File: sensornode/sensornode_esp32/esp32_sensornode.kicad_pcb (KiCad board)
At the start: 2 copper layers, 70 x 33 mm, 38 parts, among them J1 Conn_01x06_Female, J2 Conn_01x07_Male, J3 Micro_SD_Card, J4 USB_B_Mini, J5 Conn_01x02_Male, J6 Conn_02x03_Odd_Even, J7 Conn_02x03_Odd_Even, Q1 NDS3332P, Q2 NDS3332P, Q3 NDS3332P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

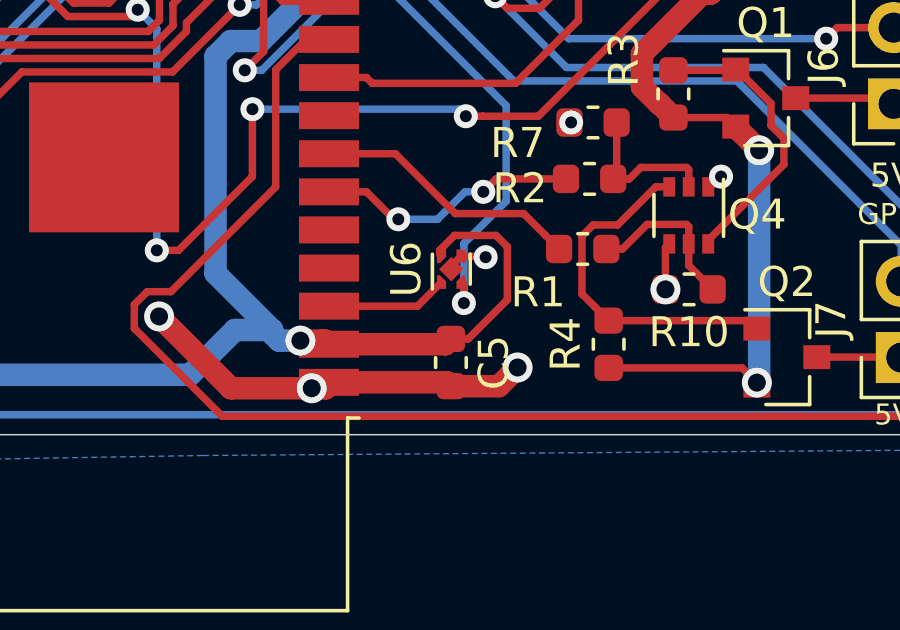
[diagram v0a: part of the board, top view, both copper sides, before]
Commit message: add lcsc part numbers
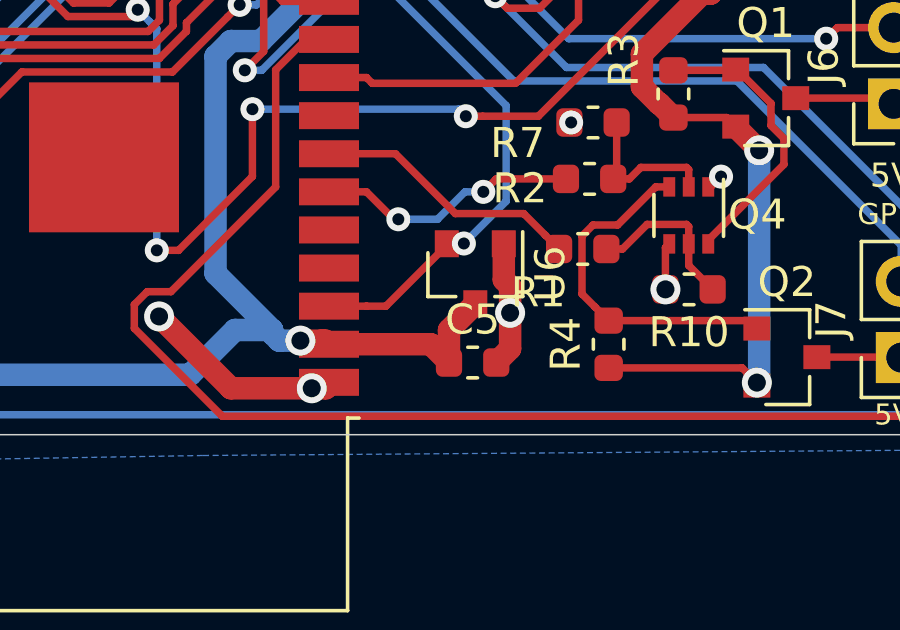
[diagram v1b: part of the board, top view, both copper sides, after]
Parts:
- C1, C4: value 2.2u -> 2.2u 10v
- C2: value 10u -> 10u 10v
- C3: value 2.2u -> 2.2u 5v
- C5: value 10u -> 10u 5v
- R5: value R -> 1.18k
- R6: value R -> 1.13k
- U6: value TPS3831 -> TPS3839DBZ; footprint Package_SON:Texas_X2SON-4_1x1mm_P0.65mm -> Package_TO_SOT_SMD:SOT-23
- moved U6 0.81 mm to (98.1, 69.6), turned to 270 degrees
- moved C5 0.72 mm to (98.0, 72.6), turned to 0 degrees
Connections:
- J1 pad 5: /~RESET -> /EN
- U6 pad 1: /EN -> GND
- U6 pad 2: /~RESET -> /EN
- U6 pad 3: GND -> +3V3
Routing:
- net /~RESET: track 77.5 -> 0.00 mm, vias 2 -> 0
- net /EN: track 4.00 -> 80.2 mm, vias 0 -> 2
- net +3V3: track 155.8 -> 151.3 mm
- net GND: track 103.1 -> 99.3 mm, vias 29 -> 28

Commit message: position file
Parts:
- J3: footprint Connector_Card:microSD_HC_Wuerth_693072010801 -> Connector_Card:microSD_HC_Hirose_DM3D-SF
- moved J3 0.95 mm to (63.1, 68.6), turned to 0 degrees
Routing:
- net GND: track 99.3 -> 115.6 mm, vias 28 -> 29
- net /CLK: track 29.5 -> 33.6 mm
- net /D2: track 28.0 -> 31.7 mm
- net /D1: track 30.8 -> 34.1 mm
- net /D3: track 29.4 -> 32.7 mm
- net /CMD: track 29.2 -> 32.3 mm
- net /D0: track 30.5 -> 33.3 mm
- net +3V3: track 151.3 -> 148.9 mm
- net +5V: track 111.4 -> 109.3 mm
- net /RxD: track 53.7 -> 52.4 mm, vias 2 -> 4
